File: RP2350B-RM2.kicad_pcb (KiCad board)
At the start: 2 copper layers, 52 x 89.5 mm, 56 parts, among them J1 10103594-0001LF, J2 Conn_01x29, J3 Conn_01x28, SW1 434133025816, SW2 434133025816, U1 RP2350B, U2 NCP1117ST33T3G, U3 W25Q128JVSIQ, U4 APS6404L-3SQR-SN, U5 RM2, X1 12MHz

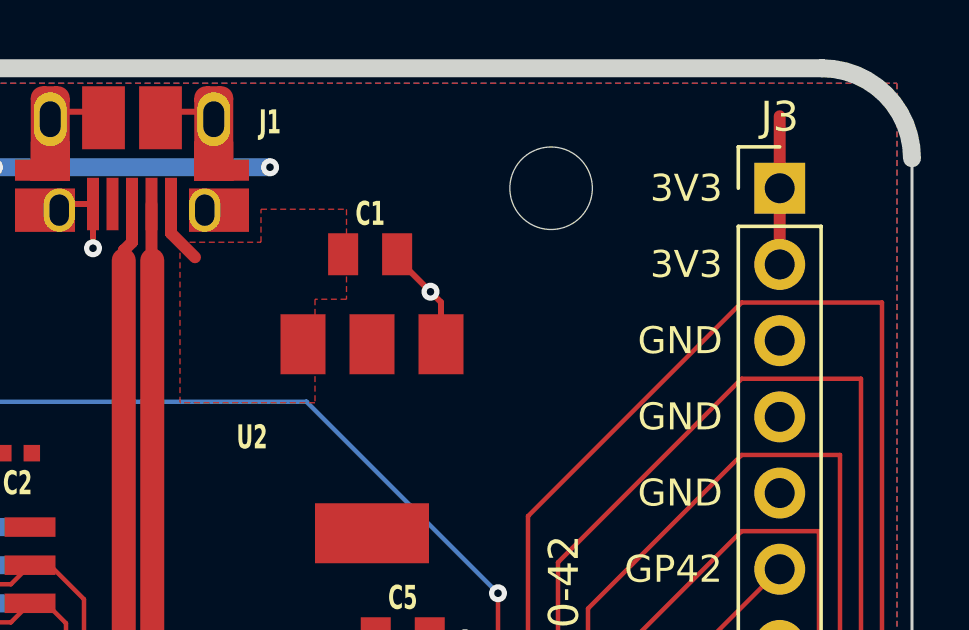
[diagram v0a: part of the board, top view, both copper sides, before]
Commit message: Add a 5 V VSYS input on J3 pin 2, with USB VBUS through a Schottky
J3 pin 2 (was a second 3V3 pin) is now VSYS, the input of the 3.3 V
regulator, so the board can run from 5 V on the header without USB.
USB VBUS reaches VSYS through D2 (B5819W, SOD-123), so header power
can't back-feed a connected computer, as on a Pico.

- Schematic: D2 between VBUS and VSYS, a VSYS power symbol and a
  PWR_FLAG; J3 pin 2's power symbol is VSYS.
- PCB: D2 sits between J1, C1 and U2. Pi's VBUS pour is split into a
  USB side (J1 to D2's anode) and VSYS. A 0.6 mm VSYS track runs from
  D2's cathode through U2's input pad, under U2 and up to J3 pin 2, so
  the 3V3 pour around J3 pin 1 stays joined to U2's output. Silkscreen
  label VSYS. layout_rm2.py reproduces the board from Pi's original.
- README power section, BOM line for D2 (LCSC C8598), renders.

DRC: 0 unconnected items, 0 schematic-parity issues. ERC: the same
pre-existing items as before.

Co-Authored-By: Claude Opus 5.5 <noreply@anthropic.com>
Claude-Session: https://claude.ai/code/session_01TVxWe2rd4mhh6Q8D57QZer
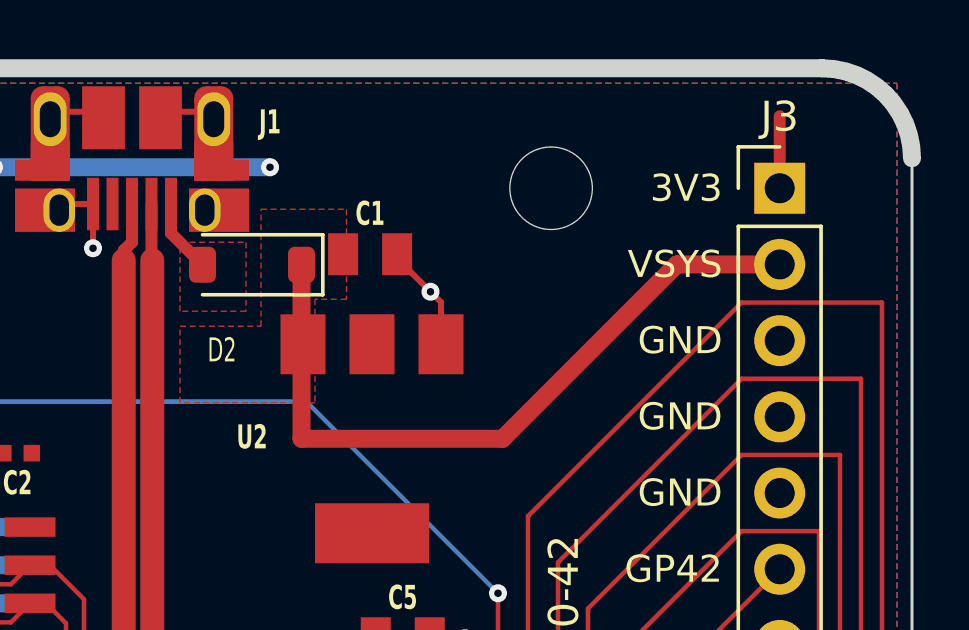
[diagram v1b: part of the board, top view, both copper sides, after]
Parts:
- added D2: B5819W, Diode_SMD:D_SOD-123, F.Cu at (104.0, 76.5)
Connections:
- C1 pad 1: VBUS -> VSYS
- J3 pad 2: +3V3 -> VSYS
- U2 pad 3: VBUS -> VSYS
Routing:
- net VSYS: track 0.00 -> 24.1 mm
- net +3V3: track 68.3 -> 65.7 mm
- added copper zone on F.Cu, net VSYS
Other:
- board text added: "VSYS"
